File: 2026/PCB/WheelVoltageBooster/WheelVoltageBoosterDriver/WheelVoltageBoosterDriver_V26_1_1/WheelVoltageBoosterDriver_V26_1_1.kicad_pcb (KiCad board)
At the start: 2 copper layers, 100 x 65 mm, 227 parts, among them J1 Conn_01x02_Pin, J10 Conn_01x03_Socket, J11 Conn_01x05_Socket, J13 Conn_01x04_Socket, J2 Conn_01x02_Pin, J3 Conn_01x04_Socket, J4 Conn_01x04_Socket, J5 Conn_01x04_Socket, J6 Conn_01x04_Socket, J7 Conn_01x02_Pin, J8 Conn_01x07_Socket, J9 Conn_01x03_Socket, SW1 SW_MEC_5E, SW2 SW_MEC_5E, U1 MAX3051, U2 LM5170QPHPTQ1, U3 STM32H523CEU6, U4 TMP235AQDCKRQ1, U5 MAX20405AFOA/VY+, U6 LD1117DT33CTR, U7 MAX20405AFOA/VY+, Y1 Crystal_GND2

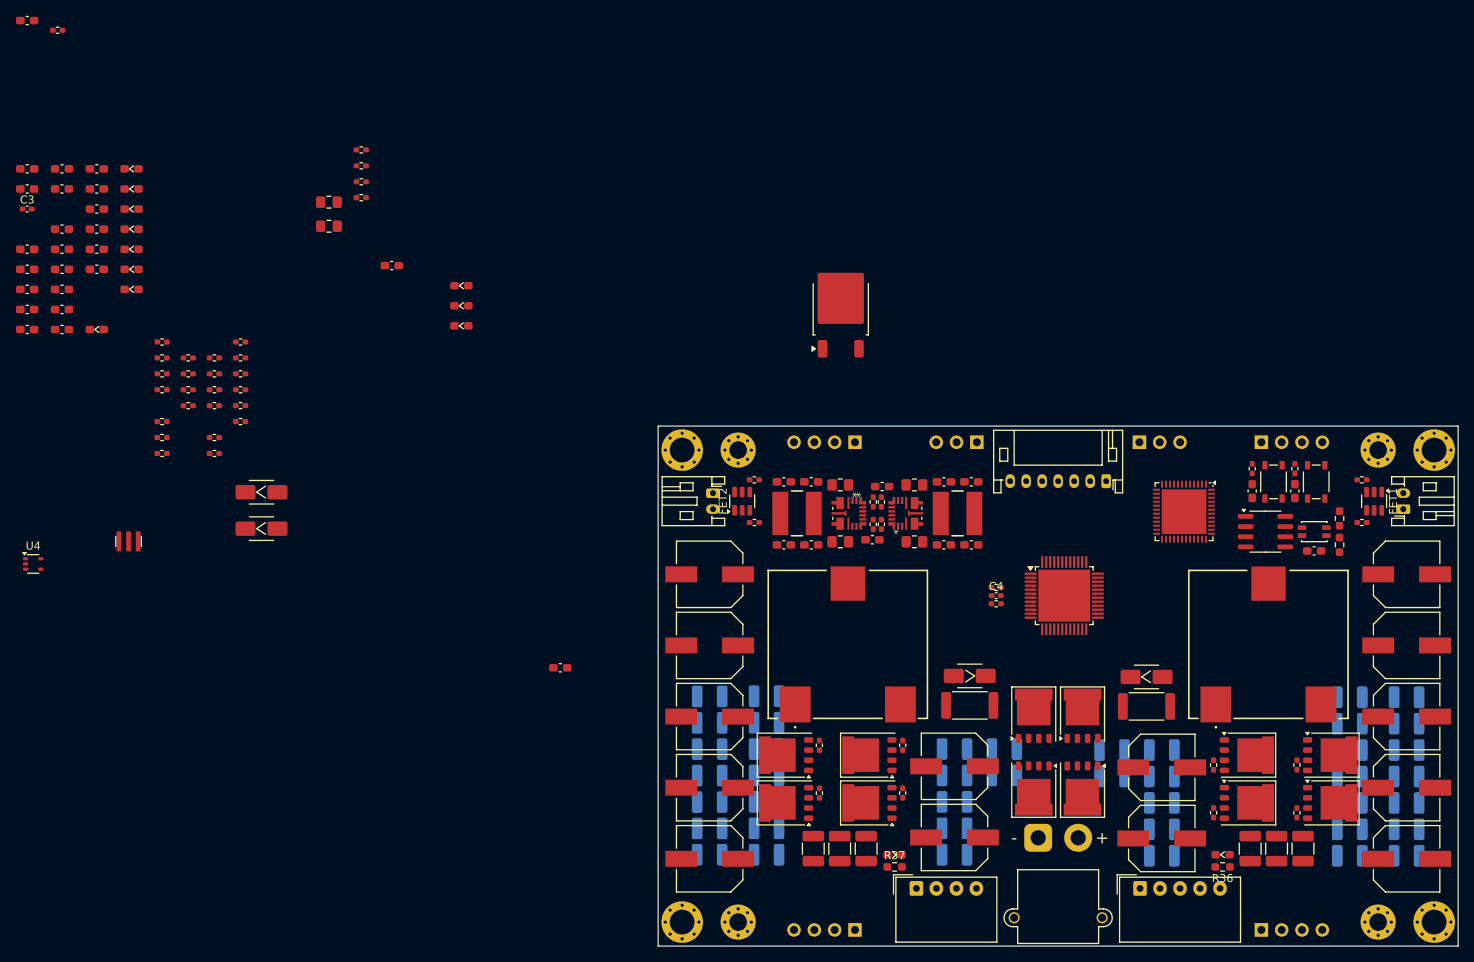
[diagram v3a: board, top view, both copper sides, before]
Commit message: 部品配置完了
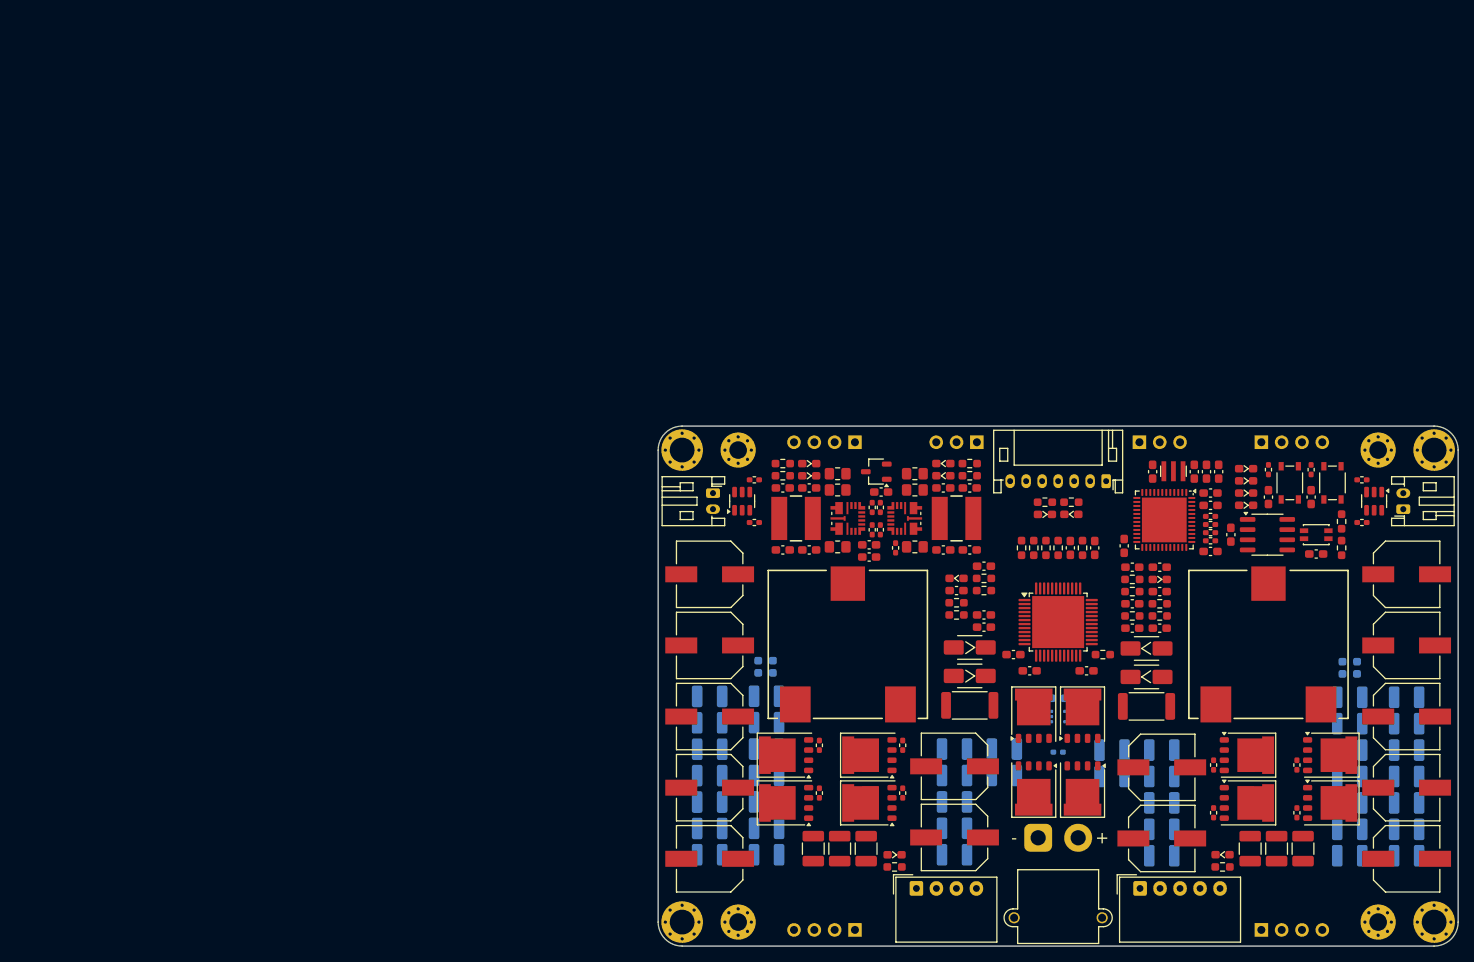
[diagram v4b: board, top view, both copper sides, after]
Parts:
- added D18: LED, WheelVoltageBooster_LIB_FTP:LED_1608_user_dif, F.Cu at (118.9, 67.2)
- added R15: 1k, Resistor_SMD:R_0603_1608Metric_Pad0.98x0.95mm_HandSolder, F.Cu at (115.6, 67.2)
- C24, R38, U4: moved to B.Cu
- C3, C4: footprint Capacitor_SMD:C_0402_1005Metric_Pad0.74x0.62mm_HandSolder -> Capacitor_SMD:C_0603_1608Metric_Pad1.08x0.95mm_HandSolder
- R1, R10, R11, R14, R17, R2, R3, R31, R32, R33, R34, R4, R5, R6, R62, R63, R64, R7, R8, R9: footprint Resistor_SMD:R_0402_1005Metric_Pad0.72x0.64mm_HandSolder -> Resistor_SMD:R_0603_1608Metric_Pad0.98x0.95mm_HandSolder
- R22, R23, R24, R25: footprint Resistor_SMD:R_0402_1005Metric_Pad0.72x0.64mm_HandSolder -> Resistor_SMD:R_0603_1608Metric_Pad0.98x0.95mm_HandSolder; moved to B.Cu
- U2: footprint Package_QFP:Texas_PHP0048E_HTQFP-48-1EP_7x7mm_P0.5mm_EP6.5x6.5mm_Mask3.62x3.62mm -> WheelVoltageBooster_LIB_FTP:LM5170QPHPTQ1
- U3: footprint Package_DFN_QFN:QFN-48-1EP_7x7mm_P0.5mm_EP5.6x5.6mm -> WheelVoltageBooster_LIB_FTP:ST32H523CEU6
- U6: value LD1117DT33CTR -> MCP1703AT-3302E/CB; footprint Package_TO_SOT_SMD:TO-252-2 -> Package_TO_SOT_SMD:TSOT-23
- moved C1 157.3 mm to (171.6, 76.1), turned to 90 degrees
- moved C40 155.4 mm to (153.6, 93.1), turned to 180 degrees
- moved R38 154.2 mm to (150.0, 103.3)
- moved C3 149.4 mm to (162.7, 83.2), turned to 180 degrees
- moved C6 148.5 mm to (162.7, 87.8), turned to 180 degrees
- moved C15 147.8 mm to (169.1, 78.2), turned to 180 degrees
- moved R24 146.3 mm to (186.4, 93.5), turned to 180 degrees
- moved C16 145.8 mm to (169.1, 70.9), turned to 180 degrees
- moved R25 145.5 mm to (186.4, 92.0)
- moved C5 145.1 mm to (159.3, 84.7), turned to 180 degrees
- moved D3 144.7 mm to (173.5, 67.8), turned to 180 degrees
- moved D4 144.7 mm to (173.5, 69.3), turned to 180 degrees
- moved C20 144.6 mm to (170.1, 68.2), turned to 90 degrees
- moved D5 144.4 mm to (173.5, 70.9), turned to 180 degrees
- moved D6 144.1 mm to (173.5, 72.4), turned to 180 degrees
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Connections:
- C25 pad 2: GND_log -> GND
- C26 pad 2: GND_log -> GND
- R26 pad 1: 3.3V_sub -> +3V3
- R35 pad 1: 3.3V_sub -> +3V3
- SW1 pad 1: GND_log -> GND
- SW1 pad 2: GND_log -> GND
- SW2 pad 1: GND_log -> GND
- SW2 pad 2: GND_log -> GND
- U1 pad 1: /CAN_TX -> CAN1_TX
- U1 pad 4: /CAN_RX -> CAN1_RX
- U3 pad 31: LED_CAN -> unconnected-(U3-PA10-Pad31)
- U3 pad 40: unconnected-(U3-PB4-Pad40) -> LED_CAN
- U3 pad 49: (no net) -> GND
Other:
- outline, holes or cut-outs redrawn

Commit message: 3Dデータ追加
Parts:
- J11: footprint Connector_Molex:Molex_SPOX_5268-05A_1x05_P2.50mm_Horizontal -> WheelVoltageBooster_LIB_FTP:Molex_SPOX_5268-05A_1x05_P2.50mm_Horizontal_ud
- J13: footprint Connector_Molex:Molex_SPOX_5268-04A_1x04_P2.50mm_Horizontal -> WheelVoltageBooster_LIB_FTP:Molex_SPOX_5268-04A_1x04_P2.50mm_Horizontal_ud
- moved C10 1.27 mm to (144.4, 89.8)
- moved C39 1.27 mm to (146.4, 91.8)
- moved C40 1.27 mm to (153.6, 91.8)
- moved R10 1.27 mm to (155.6, 89.8)
- moved U2 1.27 mm to (150.0, 85.7)
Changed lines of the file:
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@@
 		)
 	)
-	(footprint "Connector_Molex:Molex_SPOX_5268-04A_1x04_P2.50mm_Horizontal"
+	(footprint "WheelVoltageBooster_LIB_FTP:Molex_SPOX_5268-04A_1x04_P2.50mm_Horizontal_ud"
 		(layer "F.Cu")
 		(at 132.28 120.295)
@@
 			(at 3.75 -2.51 0)
 			(layer "F.SilkS")
-			(hide yes)
 			(effects
 				(font
@@
 		)
 		(embedded_fonts no)
-		(model "${KICAD9_3DMODEL_DIR}/Connector_Molex.3dshapes/Molex_SPOX_5268-04A_1x04_P2.50mm_Horizontal.step"
+		(model "${WHEELVOLTAGEBOOSTER_LIB}/WheelVoltageBooster_LIB_3D/molex_spox_4pin_h.stp"
 			(offset
-				(xyz 0 0 0)
+				(xyz 0 -9.8 1.8)
 			)
 			(scale
@@
 			)
 			(rotate
-				(xyz 0 0 0)
+				(xyz 90 -0 -0)
 			)
 		)
@@
 	(footprint "WheelVoltageBooster_LIB_FTP:LM5170QPHPTQ1"
 		(layer "F.Cu")
-		(at 150 86.999)
+		(at 150 85.729)
 		(descr "Texas PHP0048E HTQFP, 48 Pin (https://www.ti.com/lit/ds/symlink/tusb4020bi.pdf#page=42), generated with kicad-footprint-generator ipc_gullwing_generator.py")
 		(tags "Texas HTQFP QFP")
@@
 		)
 	)
-	(footprint "Connector_Molex:Molex_SPOX_5268-05A_1x05_P2.50mm_Horizontal"
+	(footprint "WheelVoltageBooster_LIB_FTP:Molex_SPOX_5268-05A_1x05_P2.50mm_Horizontal_ud"
 		(layer "F.Cu")
 		(at 160.24 120.295)
@@
 			(at 5 -2.51 0)
 			(layer "F.SilkS")
-			(hide yes)
 			(effects
 				(font
@@
 		)
 		(embedded_fonts no)
-		(model "${KICAD9_3DMODEL_DIR}/Connector_Molex.3dshapes/Molex_SPOX_5268-05A_1x05_P2.50mm_Horizontal.step"
+		(model "${WHEELVOLTAGEBOOSTER_LIB}/WheelVoltageBooster_LIB_3D/molex_spox_5pin_h.stp"
 			(offset
-				(xyz 0 0 0)
+				(xyz 0 -9.8 1.8)
 			)
 			(scale
@@
 			)
 			(rotate
-				(xyz 0 0 0)
+				(xyz 90 -0 -0)
 			)
 		)
@@
 	(footprint "Capacitor_SMD:C_0603_1608Metric_Pad1.08x0.95mm_HandSolder"
 		(layer "F.Cu")
-		(at 144.412 91.063)
+		(at 144.412 89.793)
 		(descr "Capacitor SMD 0603 (1608 Metric), square (rectangular) end terminal, IPC-7351 nominal with elongated pad for handsoldering. (Body size source: IPC-SM-782 page 76, https://www.pcb-3d.com/wordpress/wp-content/uploads/ipc-sm-782a_amendment_1_and_2.pdf), generated with kicad-footprint-generator")
 		(tags "capacitor handsolder")
@@
 	(footprint "Capacitor_SMD:C_0603_1608Metric_Pad1.08x0.95mm_HandSolder"
 		(layer "F.Cu")
-		(at 146.444 93.095)
+		(at 146.444 91.825)
 		(descr "Capacitor SMD 0603 (1608 Metric), square (rectangular) end terminal, IPC-7351 nominal with elongated pad for handsoldering. (Body size source: IPC-SM-782 page 76, https://www.pcb-3d.com/wordpress/wp-content/uploads/ipc-sm-782a_amendment_1_and_2.pdf), generated with kicad-footprint-generator")
 		(tags "capacitor handsolder")
@@
 	(footprint "Resistor_SMD:R_0603_1608Metric_Pad0.98x0.95mm_HandSolder"
 		(layer "F.Cu")
-		(at 155.588 91.063 180)
+		(at 155.588 89.793 180)
 		(descr "Resistor SMD 0603 (1608 Metric), square (rectangular) end terminal, IPC-7351 nominal with elongated pad for handsoldering. (Body size source: IPC-SM-782 page 72, https://www.pcb-3d.com/wordpress/wp-content/uploads/ipc-sm-782a_amendment_1_and_2.pdf), generated with kicad-footprint-generator")
 		(tags "resistor handsolder")
@@
 	(footprint "Capacitor_SMD:C_0603_1608Metric_Pad1.08x0.95mm_HandSolder"
 		(layer "F.Cu")
-		(at 153.556 93.095 180)
+		(at 153.556 91.825 180)
 		(descr "Capacitor SMD 0603 (1608 Metric), square (rectangular) end terminal, IPC-7351 nominal with elongated pad for handsoldering. (Body size source: IPC-SM-782 page 76, https://www.pcb-3d.com/wordpress/wp-content/uploads/ipc-sm-782a_amendment_1_and_2.pdf), generated with kicad-footprint-generator")
 		(tags "capacitor handsolder")
@@
 		)
 		(embedded_fonts no)
+		(model "${WHEELVOLTAGEBOOSTER_LIB}/WheelVoltageBooster_LIB_3D/CSTNE16M0V530000R0.STEP"
+			(offset
+				(xyz 0 0 0)
+			)
+			(scale
+				(xyz 1 1 1)
+			)
+			(rotate
+				(xyz -90 -0 -0)
+			)
+		)
 	)
 	(footprint "WheelVoltageBooster_LIB_FTP:MAX20405AFOFVY"

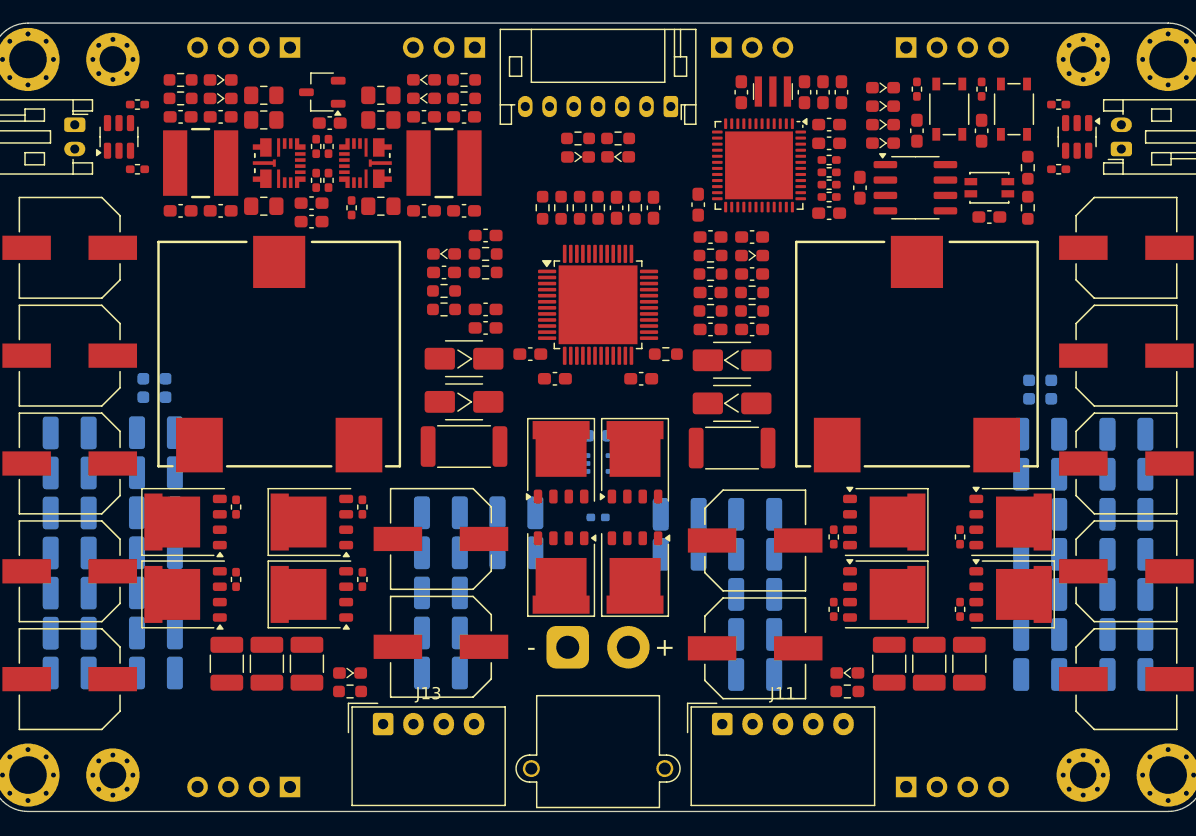
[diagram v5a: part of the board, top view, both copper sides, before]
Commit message: 昇圧系統の塗りつぶし完了
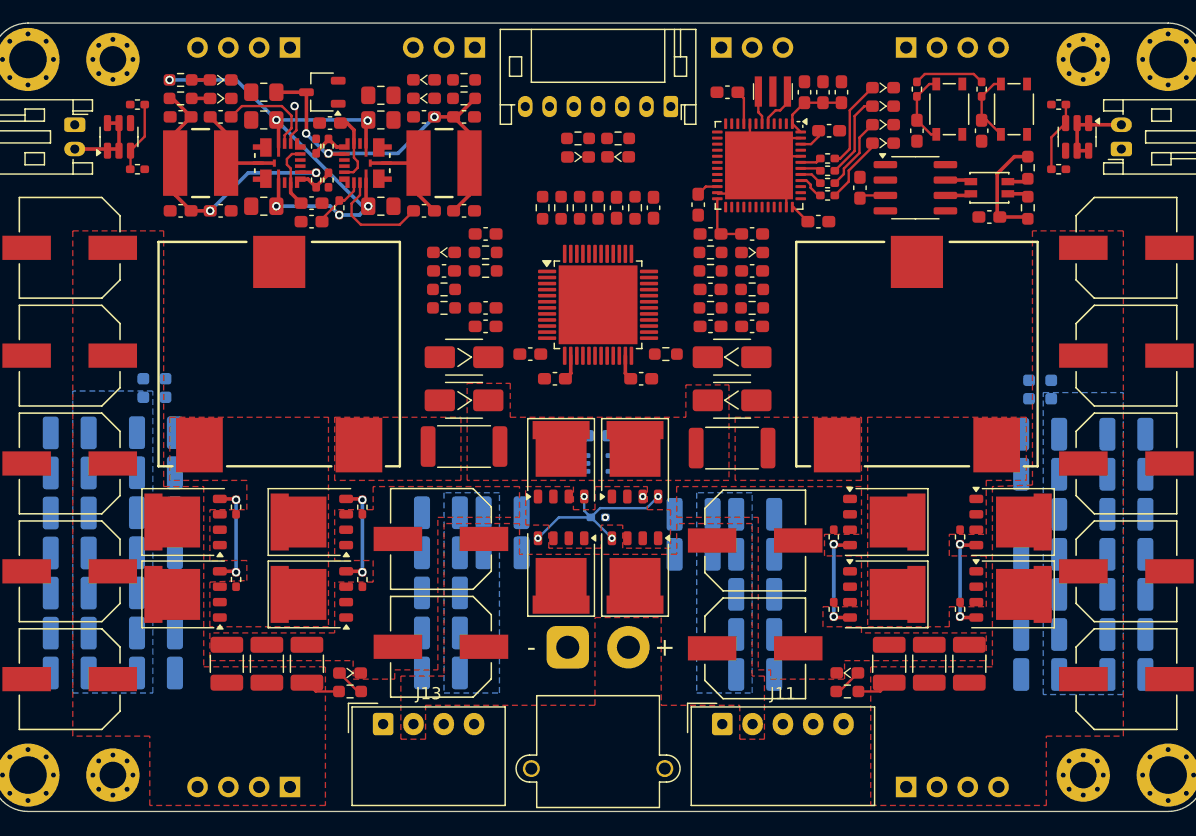
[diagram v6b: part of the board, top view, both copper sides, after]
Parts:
- removed C16: 0.1u, Capacitor_SMD:C_0603_1608Metric_Pad1.08x0.95mm_HandSolder
- moved C104 1.14 mm to (142.1, 102.9)
- moved C105 1.14 mm to (142.1, 106.2)
- moved C106 1.14 mm to (157.9, 103.0)
- moved C107 1.14 mm to (157.9, 106.3)
- moved C18 1.14 mm to (160.7, 68.2), turned to 0 degrees
- moved C15 1.13 mm to (168.2, 78.9)
- moved C21 1.03 mm to (169.1, 71.4)
- moved R61 1.02 mm to (128.7, 77.7)
- moved C14 0.25 mm to (159.3, 79.9)
- moved C19 0.25 mm to (162.7, 79.9)
- moved D1 0.25 mm to (161.0, 90.0)
- moved D14 0.25 mm to (161.0, 93.6)
- moved D7 0.25 mm to (162.7, 81.4)
- moved R31 0.25 mm to (159.3, 81.4)
- moved C3 0.25 mm to (162.7, 82.9)
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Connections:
- C25 pad 1: NRST -> nRST
- J11 pad 1: +20V -> GND
- J11 pad 2: +6V5 -> +20V
- J11 pad 3: GND -> +6V5
- J11 pad 4: CANL -> CANH
- J11 pad 5: CANH -> CANL
- J13 pad 1: +20V -> GND
- J13 pad 2: GND -> +20V
- J13 pad 3: CANL -> CANH
- J13 pad 4: CANH -> CANL
- J2 pad 1: +3V3 -> +20V
- J7 pad 1: +3V3 -> +20V
- R26 pad 2: NRST -> nRST
- SW1 pad 3: NRST -> nRST
- SW1 pad 4: NRST -> nRST
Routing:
- net +20V: track 0.00 -> 45.8 mm, vias 0 -> 6
- net +6V5: track 0.00 -> 32.5 mm, vias 0 -> 3
- net +10V: track 0.00 -> 24.2 mm, vias 0 -> 2
- net +3V3: track 0.00 -> 23.5 mm
- net GND: track 0.00 -> 20.7 mm
- net /Power_Circuit/BRKG: track 0.00 -> 15.7 mm, vias 0 -> 4
- net Net-(C12-Pad1): track 0.00 -> 9.14 mm
- net Net-(U5-BST): track 0.00 -> 8.89 mm
- net /Power_Circuit/LO2: track 0.00 -> 8.71 mm, vias 0 -> 2
- net /Power_Circuit/LO1: track 0.00 -> 8.71 mm, vias 0 -> 2
- net /Power_Circuit/HO1: track 0.00 -> 8.71 mm, vias 0 -> 2
- net /Power_Circuit/HO2: track 0.00 -> 8.71 mm, vias 0 -> 2
- net Net-(U7-BST): track 0.00 -> 8.20 mm
- net Net-(U5-LX): track 0.00 -> 7.51 mm
- net Net-(D3-A): track 0.00 -> 7.38 mm
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- added copper zone on B.Cu, net +20V
- added copper zone on F.Cu, net +20V
- added copper zone on B.Cu, net +50V
- added copper zone on F.Cu, net +50V
- added copper zone on F.Cu, net /Power_Circuit/BRKS
- added copper zone on F.Cu, net /Power_Circuit/CS1A
- added copper zone on F.Cu, net /Power_Circuit/CS1B
- added copper zone on F.Cu, net /Power_Circuit/CS2A
- added copper zone on F.Cu, net /Power_Circuit/SW1
- added copper zone on F.Cu, net /Power_Circuit/SW2
- added copper zone on F.Cu, net GND

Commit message: ん、DRC通った！！！
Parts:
- moved C3 5.72 mm to (159.3, 87.5)
- moved C8 3.75 mm to (162.7, 86.0)
- moved C24 3.56 mm to (150.0, 100.1)
- moved R11 3.05 mm to (159.3, 82.9)
- moved R4 3.05 mm to (159.3, 86.0)
- moved C11 2.17 mm to (156.7, 77.5)
- moved C13 2.17 mm to (153.7, 77.5), turned to -90 degrees
- moved R14 2.17 mm to (155.2, 77.5), turned to -90 degrees
- moved R17 2.17 mm to (152.2, 77.5)
- moved R7 2.17 mm to (150.6, 77.5)
- moved R1 1.52 mm to (162.7, 84.5)
- moved R3 1.52 mm to (162.7, 82.9)
- moved U4 1.14 mm to (150.0, 97.7), turned to -90 degrees
- moved R6 0.80 mm to (147.7, 77.5)
- moved R8 0.80 mm to (146.2, 77.5)
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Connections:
- L1 pad 3: (no net) -> GND
- L2 pad 3: (no net) -> GND
- U3 pad 12: IOUT1 -> IOUT2
- U3 pad 13: IOUT2 -> IOUT1
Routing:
- net +20V: track 45.8 -> 165.2 mm, vias 6 -> 41
- net +10V: track 24.2 -> 130.7 mm, vias 2 -> 8
- net +6V5: track 32.5 -> 128.9 mm, vias 3 -> 6
- net FET_FAN: track 0.00 -> 96.2 mm, vias 0 -> 6
- net +3V3: track 23.5 -> 116.4 mm, vias 0 -> 3
- net CANH: track 1.75 -> 93.5 mm, vias 0 -> 1
- net CANL: track 1.75 -> 91.7 mm, vias 0 -> 1
- net GND: track 20.7 -> 90.2 mm, vias 0 -> 43
- net VM_SCAN2: track 0.00 -> 58.1 mm, vias 0 -> 3
- net /Power_Circuit/HO1: track 8.71 -> 48.9 mm, vias 2 -> 3
- net VM_SCAN1: track 0.00 -> 39.7 mm, vias 0 -> 3
- net +50V: track 5.78 -> 44.6 mm, vias 0 -> 62
- net 10VEN: track 3.34 -> 40.1 mm, vias 1 -> 2
- net /Power_Circuit/HO2: track 8.71 -> 44.6 mm, vias 2 -> 3
- net /Power_Circuit/CS1B: track 0.00 -> 33.5 mm, vias 0 -> 4
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- added copper zone on B.Cu, net +3V3
- added copper zone on F.Cu, net +3V3
- added copper zone on B.Cu, net GND

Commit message: ビア打ち終わり
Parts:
- C27, C29, C31, C33: value 180u -> 220u
- C41, C43, C45, C47, C49, C51, C53, C55, C57, C59: value 47u -> 68u
- J10, J9: footprint Connector_PinSocket_2.54mm:PinSocket_1x03_P2.54mm_Vertical -> WheelVoltageBooster_LIB_FTP:PinSocket_1x03_P2.54mm_Vertical_ud
- J3, J4, J5, J6: footprint Connector_PinSocket_2.54mm:PinSocket_1x04_P2.54mm_Vertical -> WheelVoltageBooster_LIB_FTP:PinSocket_1x04_P2.54mm_Vertical_ud
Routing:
- net +20V: track 165.2 -> 186.5 mm, vias 41 -> 39
- net GND: track 90.2 -> 70.2 mm, vias 43 -> 316
- net +3V3: track 116.4 -> 109.3 mm, vias 3 -> 9
- net +10V: track 130.7 -> 124.5 mm
- net VM_SCAN1: track 39.7 -> 44.1 mm
- net VM_SCAN2: track 58.1 -> 62.4 mm
- net Net-(U7-LX): track 7.38 -> 4.88 mm
- net +50V: track 44.6 -> 46.9 mm
- net /Power_Circuit/LO1: track 41.1 -> 39.8 mm
- net /Power_Circuit/HO1: track 48.9 -> 48.0 mm
- net Net-(U3-PH0-OSC_IN): track 3.53 -> 2.58 mm
- net +6V5: track 128.9 -> 129.7 mm
- net Net-(U2-OPT): track 18.2 -> 17.5 mm
- net Net-(C12-Pad1): track 9.24 -> 8.65 mm
- net USART1_TX: track 25.5 -> 24.9 mm
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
